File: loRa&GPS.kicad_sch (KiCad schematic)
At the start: 13 parts, among them J4 Conn_Coaxial, U10 RAK3172, U3 STA8135GA, U9 TESEO-LIV4F

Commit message: lib allign
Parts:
- BT1: footprint (none) -> Battery:BatteryHolder_Seiko_MS621F
- D8: footprint (none) -> Diode_SMD:D_0603_1608Metric_Pad1.05x0.95mm_HandSolder
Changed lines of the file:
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@@
 			)
 		)
-		(property "Footprint" ""
+		(property "Footprint" "Battery:BatteryHolder_Seiko_MS621F"
 			(at 99.568 46.228 90)
 			(effects
@@
 			)
 		)
-		(property "Footprint" ""
+		(property "Footprint" "Diode_SMD:D_0603_1608Metric_Pad1.05x0.95mm_HandSolder"
 			(at 99.568 25.654 90)
 			(effects

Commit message: Aggiornamento routing
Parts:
- removed AE1: Antenna_Shield, symbol Device:Antenna_Shield
- removed C25, C26: 100nF, Capacitor_SMD:C_0603_1608Metric_Pad1.08x0.95mm_HandSolder, symbol Device:C
- removed U3: STA8135GA, footprints:TFBGA160_7X11X1p2_STM, symbol 2025-11-15_15-30-48:STA8135GA
- added ANT1: AANI-PP-0055, AANIPP0055, symbol AANI-PP-0055:AANI-PP-0055
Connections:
- net at U9.11 (RF_IN): now also ANT1.1
- no-connect marks 19 -> 28
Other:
- moved on the sheet: BT1, C37, C39, C40, D8, J4, R39, U10, U9

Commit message: fix continuo
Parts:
- ANT1: footprint AANIPP0055 -> antenna_GPS:AANIPP0055
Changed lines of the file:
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@@
 			)
 		)
-		(property "Footprint" "AANIPP0055"
+		(property "Footprint" "antenna_GPS:AANIPP0055"
 			(at 141.91 31.75 0)
 			(effects

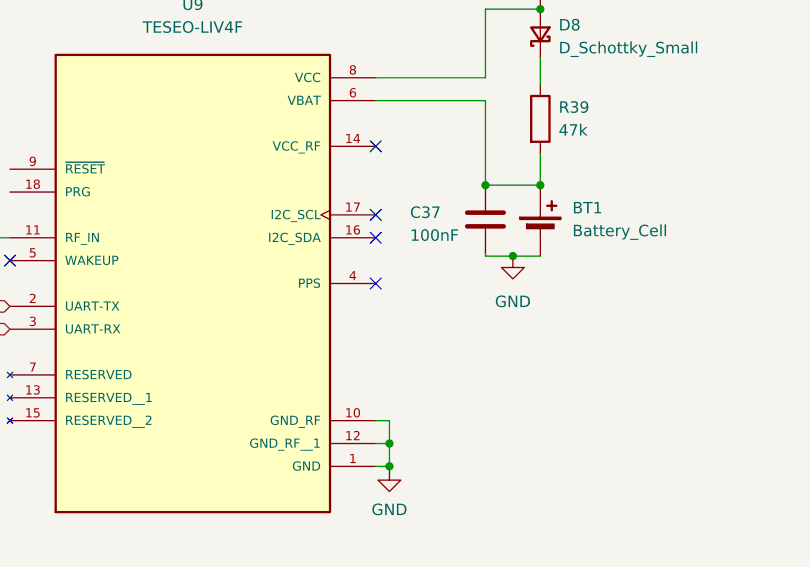
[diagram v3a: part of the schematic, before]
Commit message: 10/01/2025
1v1 fix and v regulator final decision, general BOM corrections and allignments
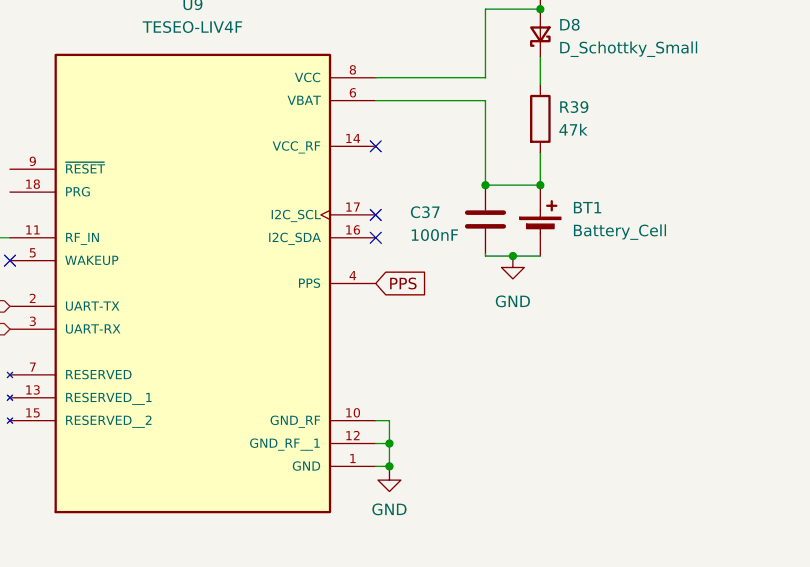
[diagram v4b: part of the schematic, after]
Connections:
- net PPS: now reaches U9.4 (PPS)
- no-connect marks 28 -> 27
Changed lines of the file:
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@@
-	)
-	(no_connect
-		(at 105.41 67.31)
 	)
 	(no_connect
@@
 				(hide yes)
 			)
+		)
+	)
+	(global_label "PPS"
+		(shape input)
+		(at 105.41 67.31 0)
+		(fields_autoplaced yes)
+		(effects
+			(font
+				(size 1.27 1.27)
+			)
+			(justify left)
+		)
+		(property "Intersheetrefs" "${INTERSHEET_REFS}"
+			(at 112.1447 67.31 0)
+			(effects
+				(font
+					(size 1.27 1.27)
+				)
+				(justify left)
+				(hide yes)
+			)

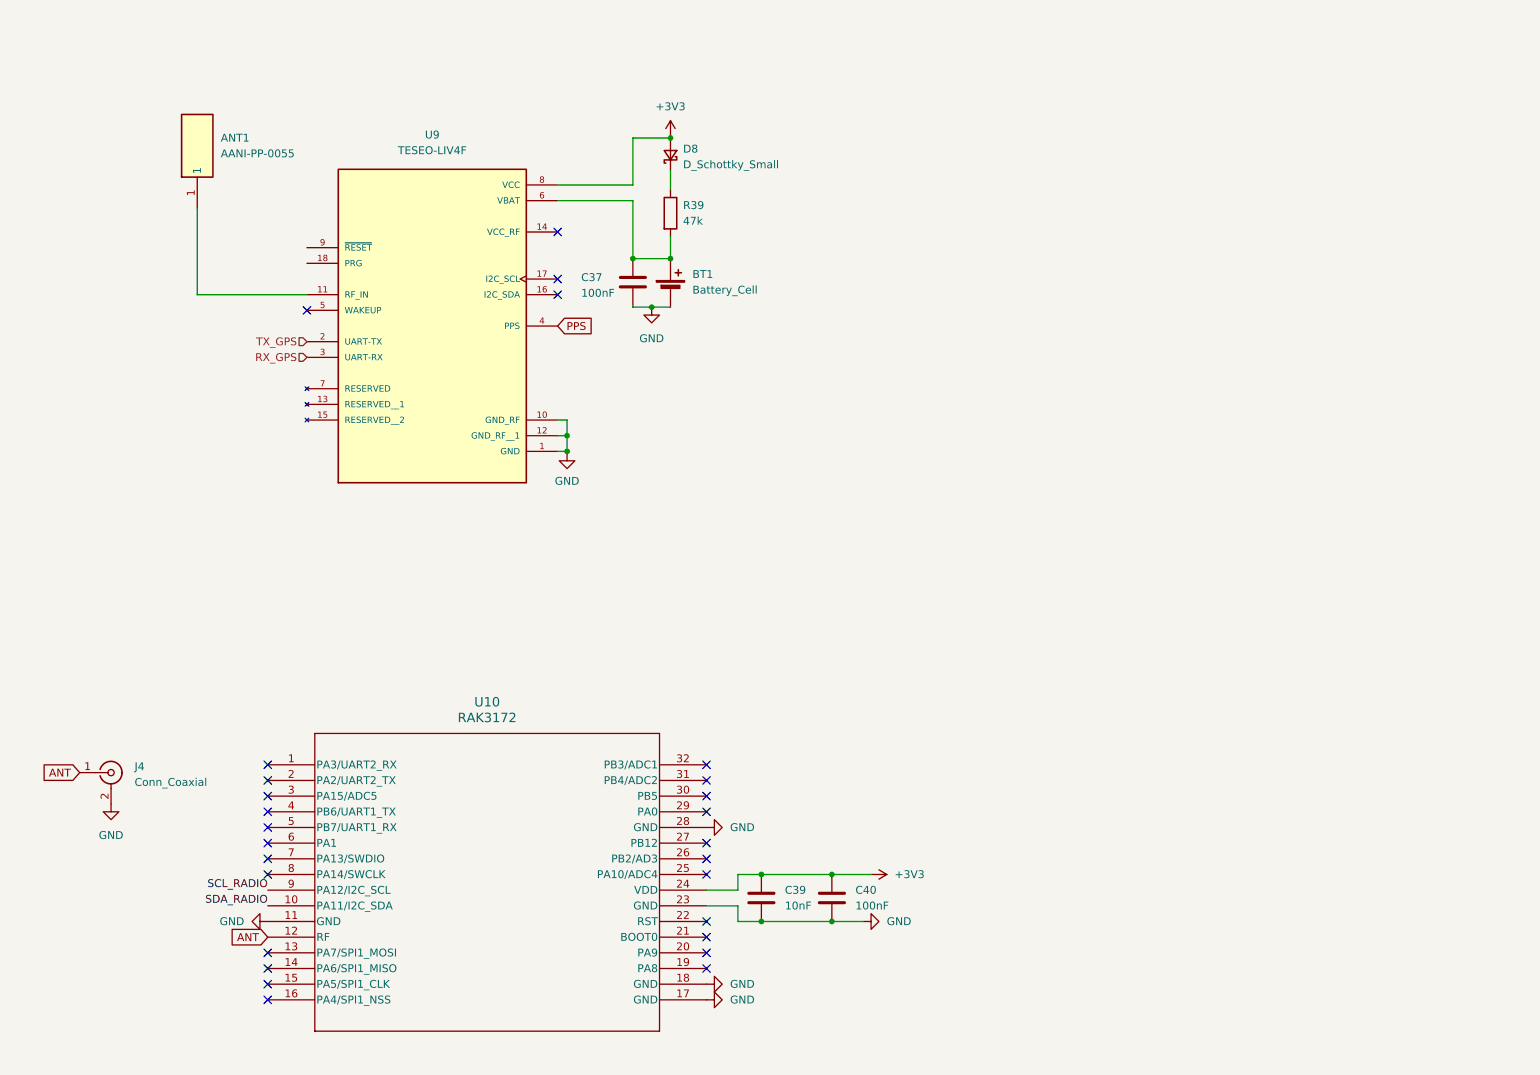
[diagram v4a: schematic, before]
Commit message: Small changes
modified Main LEDs.
Added Radio LEDs.

Connected the GPS uart to the Radio.
Added a test point for the GPS PRG pin.

Modified the Pyro current limiter for better BOM compliance.

Modified a copule of estetic things on the schematic.
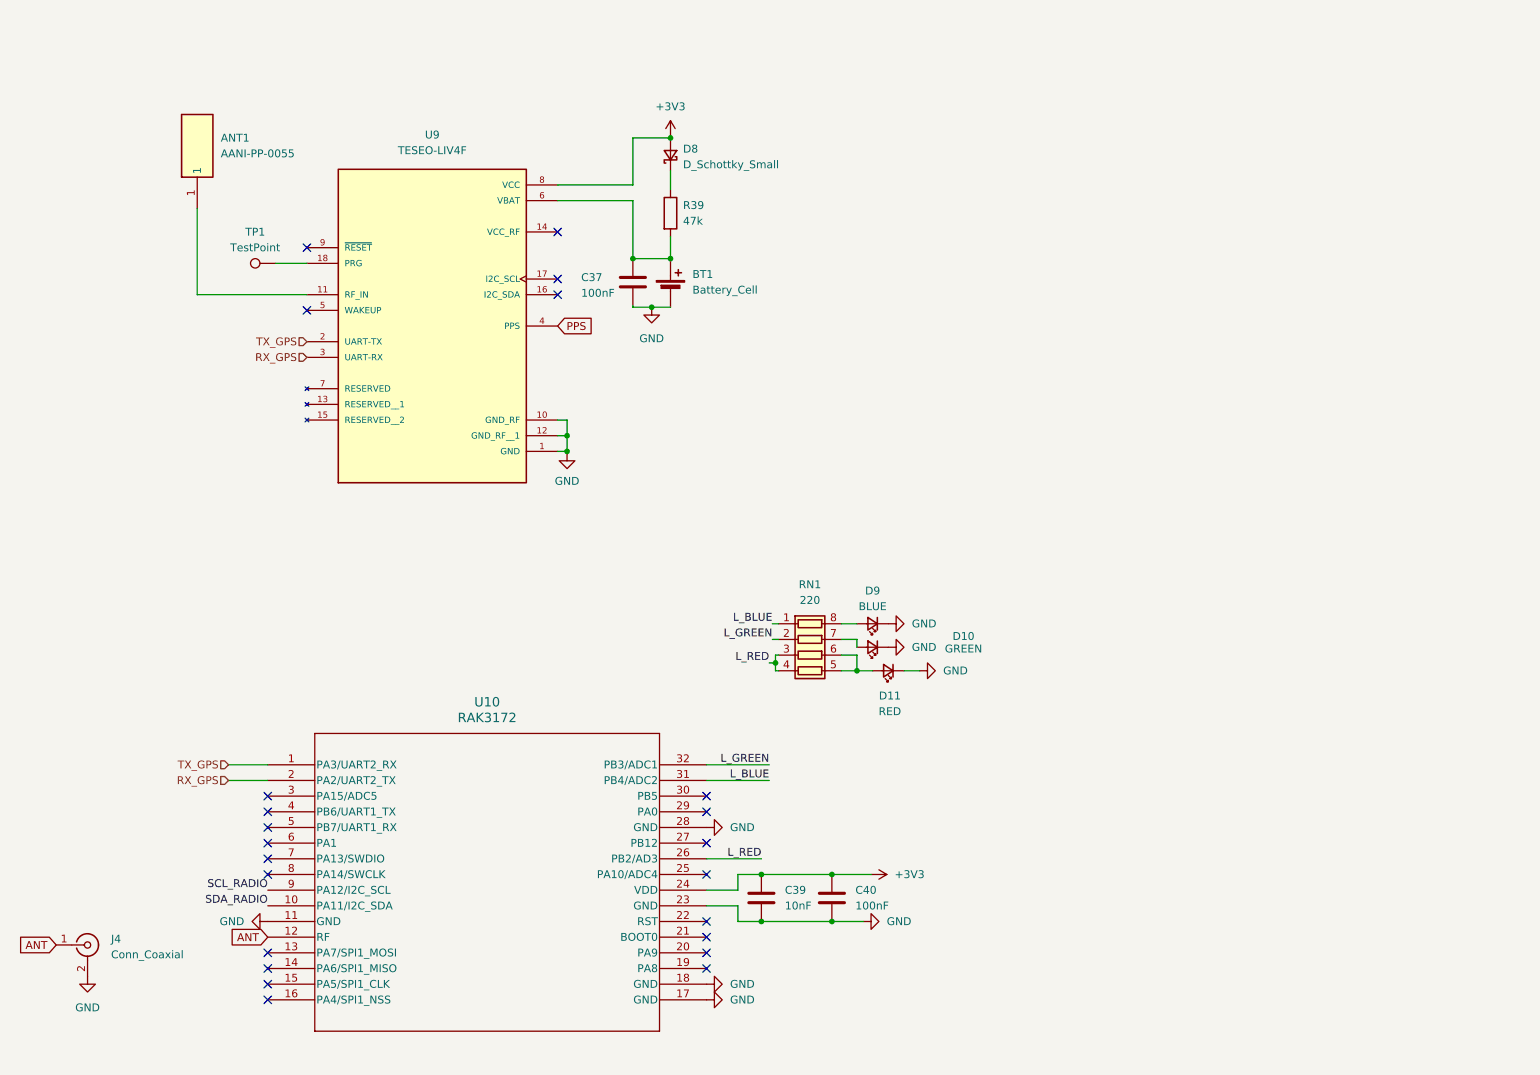
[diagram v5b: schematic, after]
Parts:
- added D10: GREEN, LED_SMD:LED_0603_1608Metric, symbol Device:LED_Small
- added D11: RED, LED_SMD:LED_0603_1608Metric, symbol Device:LED_Small
- added D9: BLUE, LED_SMD:LED_0603_1608Metric, symbol Device:LED_Small
- added RN1: 220, Resistor_SMD:R_Array_Convex_4x0603, symbol Device:R_Pack04
- added TP1: TestPoint, TestPoint:TestPoint_Pad_D1.0mm, symbol Connector:TestPoint
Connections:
- net GND: now also D10.1 (K), D11.1 (K), D9.1 (K)
- net RX_GPS: now also U10.2 (PA2/UART2_TX)
- net TX_GPS: now also U10.1 (PA3/UART2_RX)
- net L_RED: now reaches U10.26 (PB2/AD3)
- net L_RED: now also RN1.3 (R3.1), RN1.4 (R4.1)
- net L_BLUE: now reaches U10.31 (PB4/ADC2)
- net L_BLUE: now also RN1.1 (R1.1)
- net L_GREEN: now reaches U10.32 (PB3/ADC1)
- net L_GREEN: now also RN1.2 (R2.1)
- net at U9.18 (PRG): now also TP1.1
- new net: D11.2 (A), RN1.5 (R4.2), RN1.6 (R3.2)
- new net: D10.2 (A), RN1.7 (R2.2)
- new net: D9.2 (A), RN1.8 (R1.2)
- no-connect marks 27 -> 23
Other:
- moved on the sheet: J4

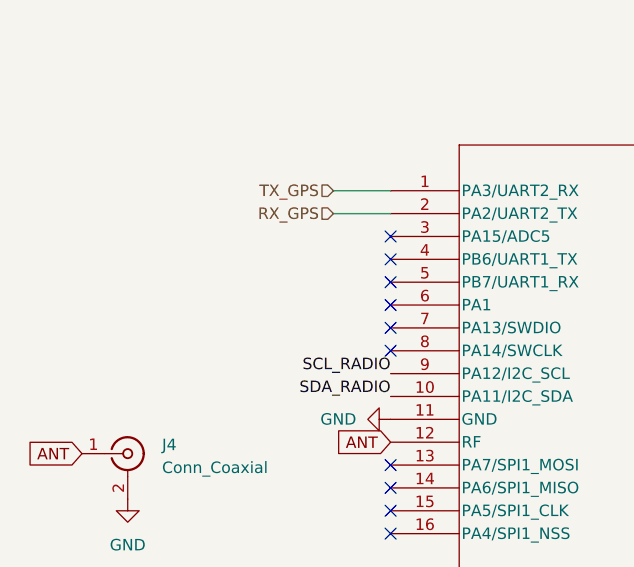
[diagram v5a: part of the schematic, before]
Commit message: Small details
Added SWD test point for the Radio.
Added UART test point for the Radio.

Connected the GPS to the radio trough UART.
Fixed names around the board.
Checked the Crystal capacitance (OK).
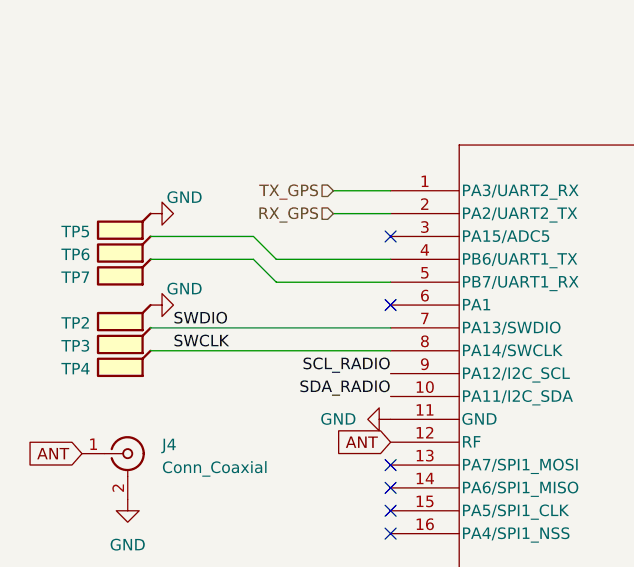
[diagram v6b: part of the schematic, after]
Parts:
- added TP2, TP3, TP4, TP5, TP6, TP7: TestPoint_Flag, TestPoint:TestPoint_Pad_2.0x2.0mm, symbol Connector:TestPoint_Flag
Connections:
- net GND: now also TP2.1, TP5.1
- net at U10.4 (PB6/UART1_TX): now also TP6.1
- net at U10.5 (PB7/UART1_RX): now also TP7.1
- net SWDIO: now reaches U10.7 (PA13/SWDIO)
- net SWDIO: now also TP3.1
- net SWCLK: now reaches U10.8 (PA14/SWCLK)
- net SWCLK: now also TP4.1
- no-connect marks 23 -> 19

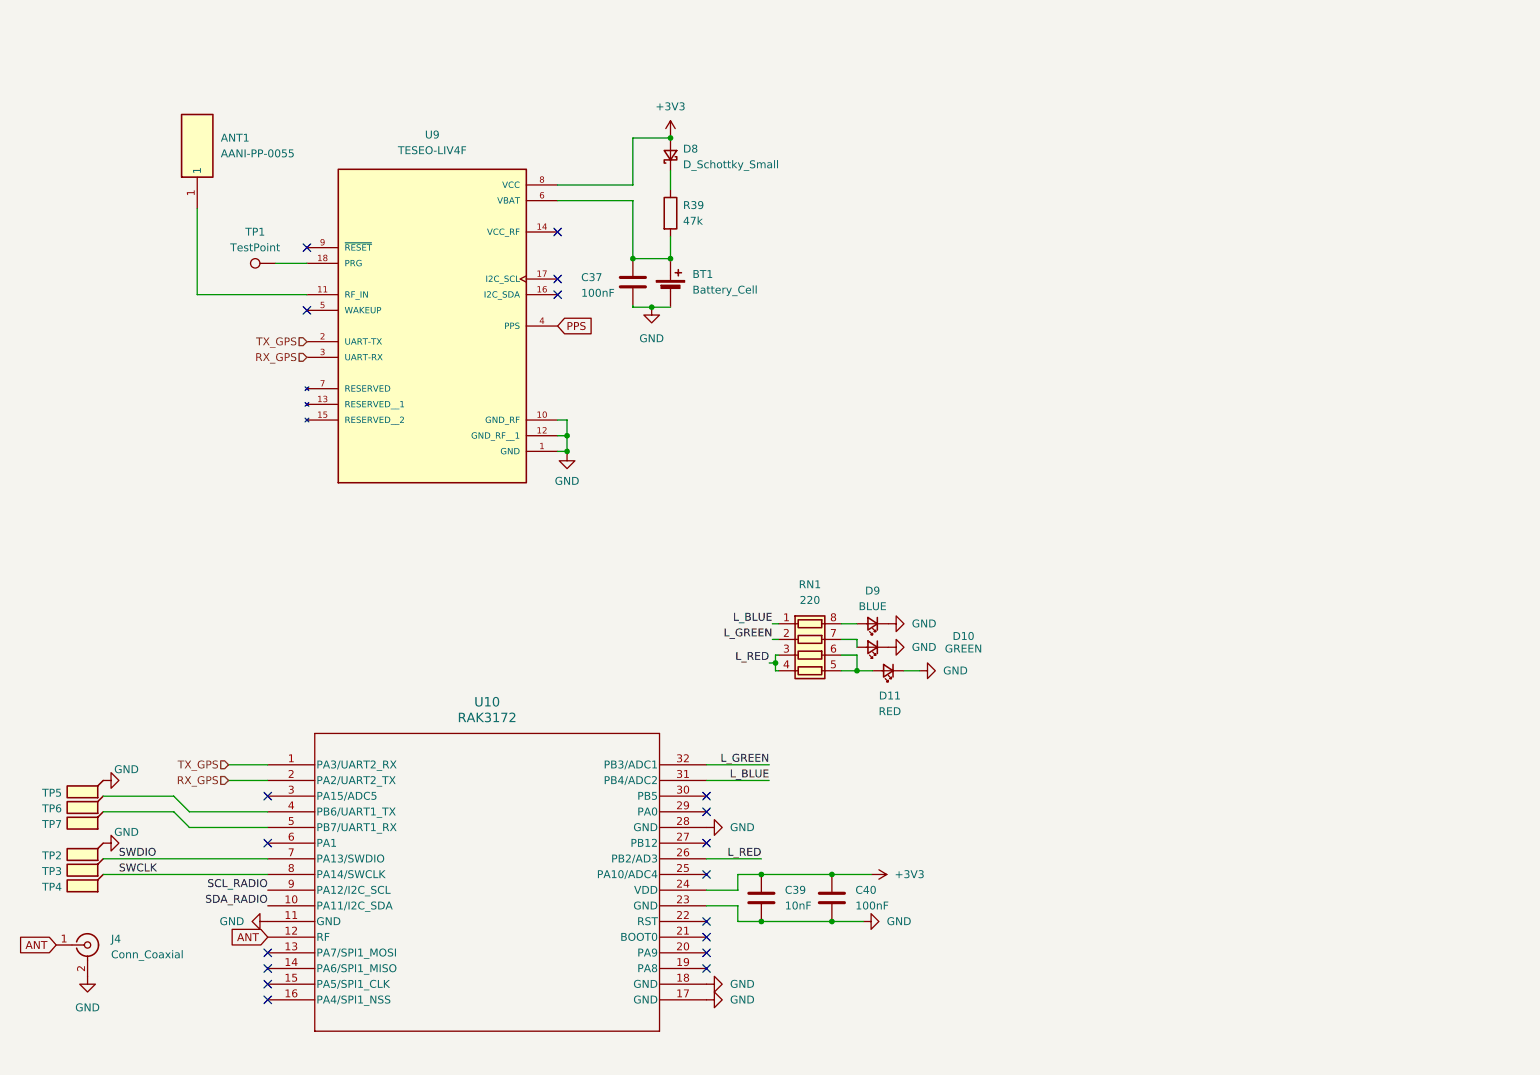
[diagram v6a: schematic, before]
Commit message: Last fixes
Added i2c connection to gps.
Added test point for swd and Uart for radio.
check footprint compatibility between liv3f and liv4f.
... Other ...
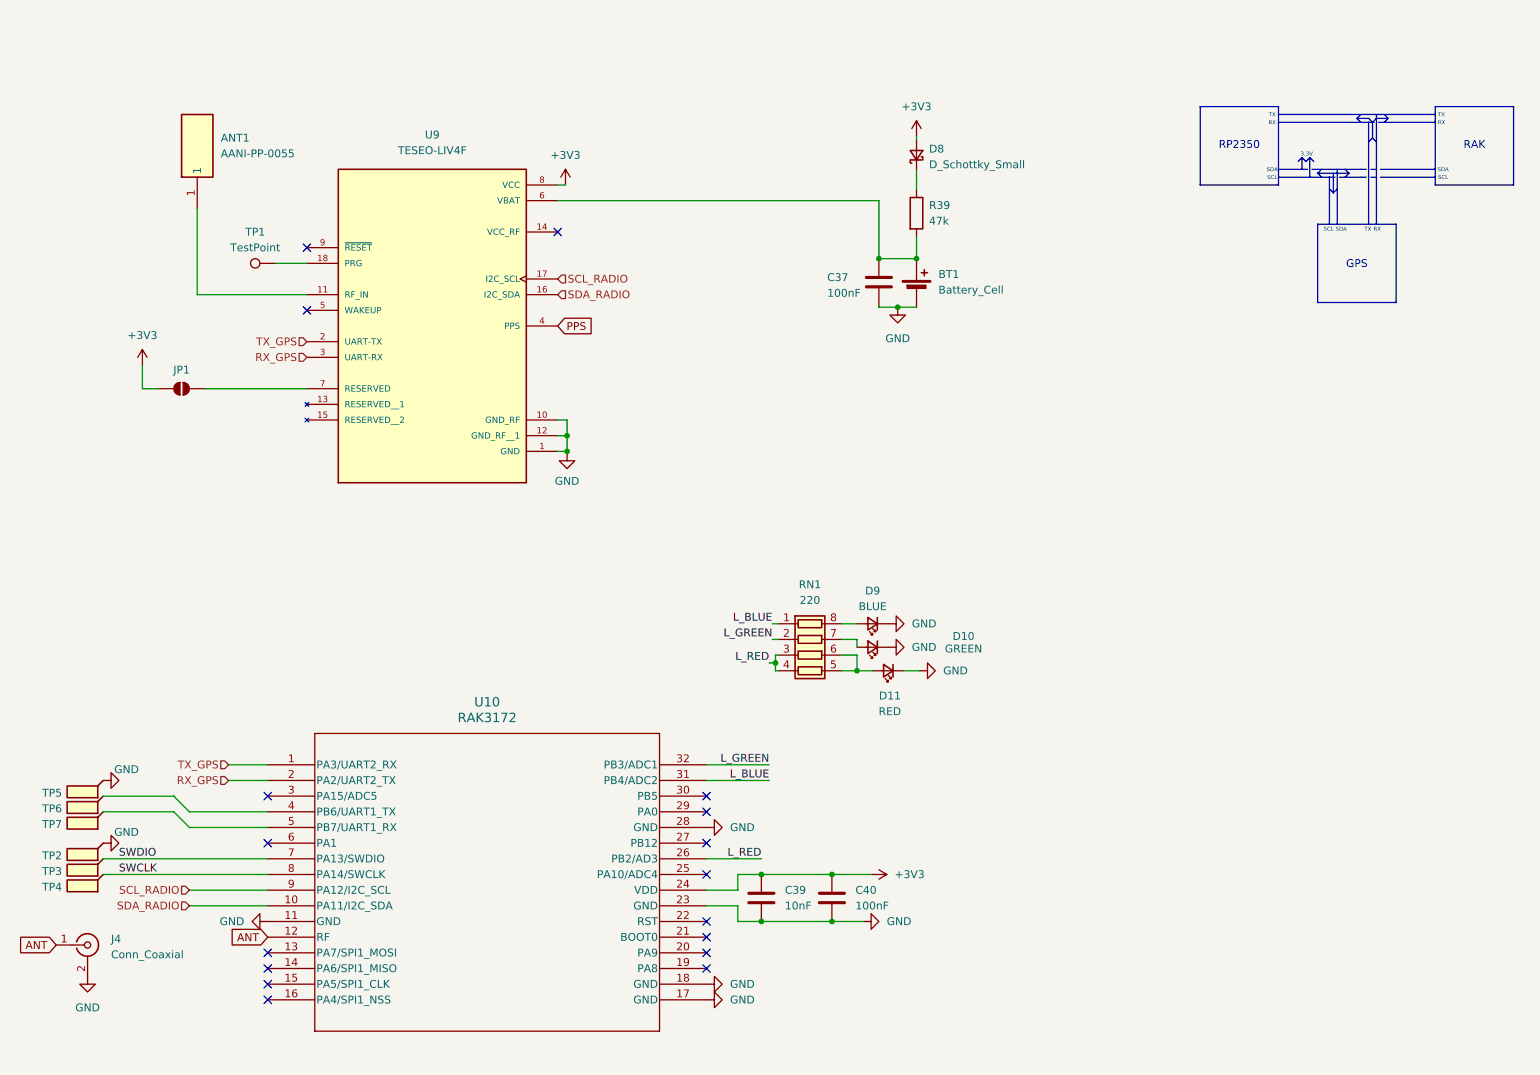
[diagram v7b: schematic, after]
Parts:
- added JP1: SolderJumper_2_Open, Jumper:SolderJumper-2_P1.3mm_Open_TrianglePad1.0x1.5mm, symbol Jumper:SolderJumper_2_Open
- U9: footprint TESEO_LIV4F:XCVR_TESEO-LIV4F -> TESEO-LIV4F:XCVR_TESEO-LIV4F
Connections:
- net +3V3: now also JP1.2 (B)
- net SCL_RADIO: now also U9.17 (I2C_SCL)
- net SDA_RADIO: now also U9.16 (I2C_SDA)
- net at U9.7 (RESERVED): now also JP1.1 (A)
- no-connect marks 19 -> 17
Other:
- note added: "3.3V"
- note added: "GPS"
- note added: "RAK"
- note added: "RP2350"
- note added: "RX"
- note added: "SCL"
- note added: "SDA"
- note added: "TX"
- moved on the sheet: BT1, C37, D8, R39
